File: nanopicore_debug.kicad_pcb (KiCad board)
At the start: 4 copper layers, 40 x 40 mm, 27 parts, among them J1 NanoPi_Core_GPIO2, J2 NanoPi_Core_GPIO1, J3 NanoPi_Core_GPIO3, J4 USB_B_Micro_DEBUG, J5 USB_A, U1 AMS1117-3.3, U2 CH340G, U3 SRV05-4, Y1 12MHz

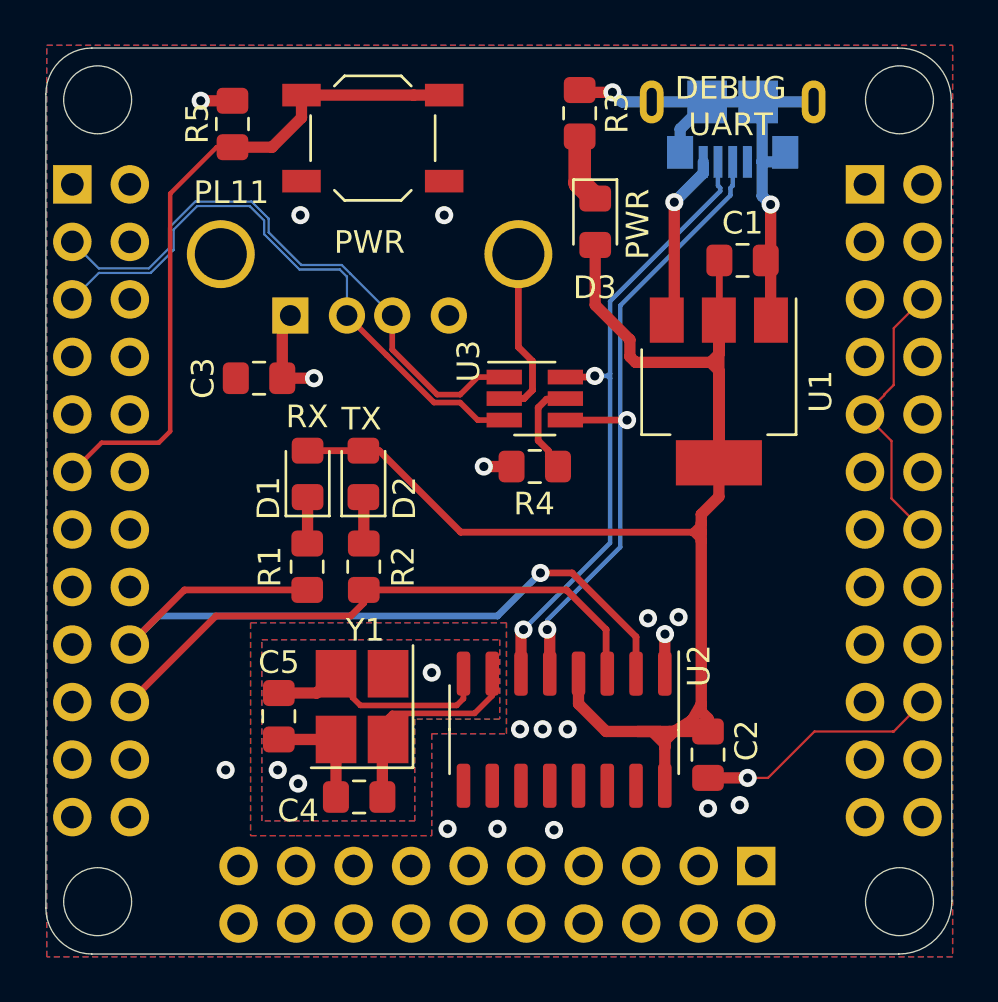
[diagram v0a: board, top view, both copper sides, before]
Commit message: Exports and initial BOM
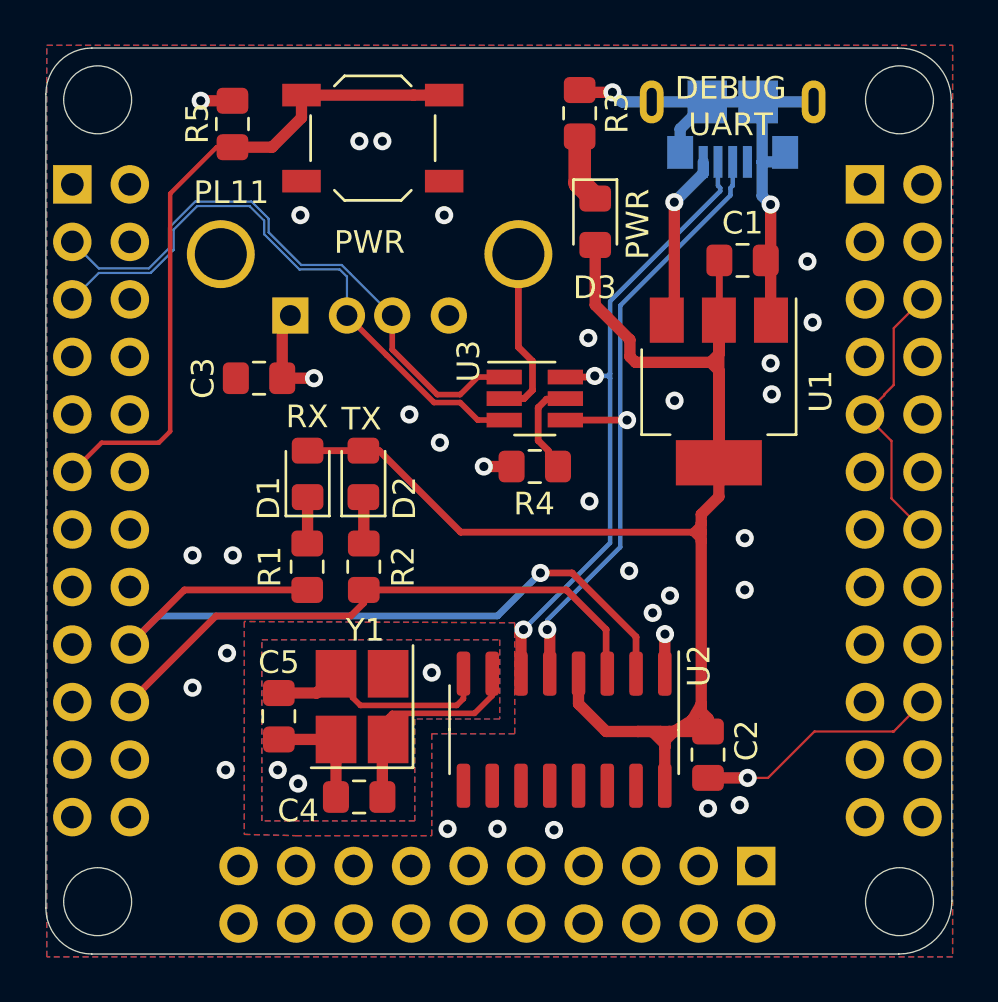
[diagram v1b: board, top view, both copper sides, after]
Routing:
- net GND: vias 20 -> 35

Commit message: Add 0R resistor to power CH340 from NanoPi
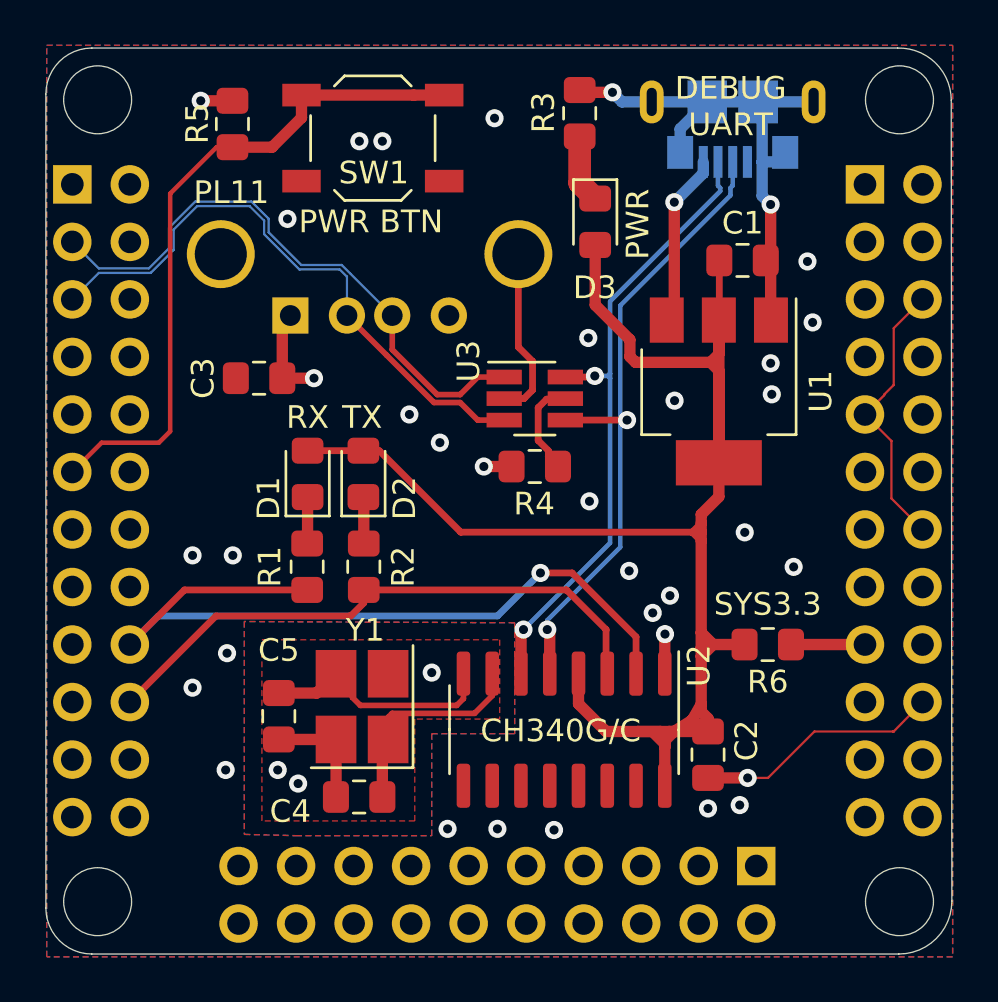
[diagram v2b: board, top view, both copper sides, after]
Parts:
- removed PWR: SW_PWR, Button_Switch_SMD:SW_SPST_TL3342
- added R6: 0, Resistor_SMD:R_0805_2012Metric_Pad1.15x1.40mm_HandSolder, F.Cu at (100.8, 69.0)
- added SW1: SW_PWR, Button_Switch_SMD:SW_SPST_TL3342, F.Cu at (83.4, 46.6)
- U2: value CH340G -> CH340G/C
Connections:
- J2 pad 17: Net-(J2-Pad17) -> VDD_3.3V
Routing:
- net Net-(C1-Pad1): track 76.7 -> 80.3 mm
- net VDD_3.3V: track 0.00 -> 3.27 mm
- removed copper zone on In2.Cu, net GND
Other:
- board text added: "PWR BTN"
- board text added: "SYS3.3"

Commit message: Update BOM
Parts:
- D1: value LED_DEBUG_TXD -> LED_RED
- D2: value LED_DEBUG_RXD -> LED_RED
- D3: value LED_DEBUG_PWR -> LED_RED
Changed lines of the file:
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@@
   (title_block
     (title "NanoPI NEO Core debug shield")
+    (date 2020-06-22)
+    (rev v2)
   )
   (layers
@@
       (effects (font (size 1 1) (thickness 0.15)))
     )
-    (fp_text value LED_DEBUG_PWR (at 0 1.65 90) (layer F.Fab)
+    (fp_text value LED_RED (at 0 1.65 90) (layer F.Fab)
       (effects (font (size 1 1) (thickness 0.15)))
     )
@@
       (effects (font (size 1 1) (thickness 0.15)))
     )
-    (fp_text value LED_DEBUG_RXD (at 0 1.65 90) (layer F.Fab)
+    (fp_text value LED_RED (at 0 1.65 90) (layer F.Fab)
       (effects (font (size 1 1) (thickness 0.15)))
     )
@@
       (effects (font (size 1 1) (thickness 0.15)))
     )
-    (fp_text value LED_DEBUG_TXD (at 0 1.65 90) (layer F.Fab)
-      (effects (font (size 1 1) (thickness 0.15)))
-    )
+    (fp_text value LED_RED (at 0 1.65 90) (layer F.Fab)
+      (effects (font (size 1 1) (thickness 0.15)))
+    )
